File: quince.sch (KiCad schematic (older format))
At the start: 26 parts, among them J1 NEIGHBOR1, J2 NEIGHBOR2, J7 BONUS_ROW, P9 BASEBAND, U1 TLV3502

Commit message: updated to KiCad 5.1
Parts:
- C1: symbol C -> Device:C
- J1, J2: symbol CONN_02X20 -> Connector_Generic:Conn_02x20_Odd_Even
- J7: symbol CONN_01X20 -> Connector_Generic:Conn_01x20
- MH1, MH2, MH3, MH4: symbol CONN_01X01 -> Connector_Generic:Conn_01x01
- P9: symbol CONN_02X08 -> Connector_Generic:Conn_02x08_Odd_Even
- R1, R10, R11, R12, R13, R14, R15, R16, R2, R3, R4, R5, R6, R7, R8, R9: symbol R -> Device:R
- U1: symbol TLV3502 -> gsg-symbols:TLV3502
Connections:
- wire segments 169 -> 188

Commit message: add RF section to schematic copied from Daisho/rx2400ism
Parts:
- removed P9: BASEBAND, gsg-modules:HEADER-2x8, symbol Connector_Generic:Conn_02x08_Odd_Even
- removed R10, R11, R12, R13, R14, R15, R16, R7, R8, R9: R, gsg-modules:0603, symbol Device:R
- added C? (x8): 100nF, symbol Device:C
- added C? (x4): 18pF, symbol Device:C
- added C? (x4): 68pF, symbol Device:C
- added C? (x10): 100pF, symbol Device:C
- added C? (x2): 1pF, symbol Device:C
- added C? (x2): 470pF, symbol Device:C
- added D?: D_TVS, symbol Device:D_TVS
- added FB?: Ferrite_Bead, symbol Device:Ferrite_Bead
- added J? (x2): RFIN, symbol Connector:Conn_Coaxial
- added J?: GND, symbol Connector_Generic:Conn_01x02
- added J? (x11): Conn_01x01, symbol Connector_Generic:Conn_01x01
- added L? (x5): 470nH, symbol Device:L
- added L? (x2): 680nH, symbol Device:L
- added R? (x2): 10k, symbol Device:R
- added R? (x5): 0, symbol Device:R
- added R? (x4): 100, symbol Device:R
- added R? (x2): 2k2, symbol Device:R
- added R? (x2): 3k3, symbol Device:R
- added R? (x2): 200, symbol Device:R
- added R?: 0, gsg-modules:0603, symbol Device:R
- added U2: AD8347, symbol gsg-symbols:AD8347
- added U3: B9413, symbol gsg-symbols:B9413
- added U4: MAX2641, symbol gsg-symbols:MAX2641
- added U5: 2450BP39D100CE, symbol gsg-symbols:2450BP39D100CE
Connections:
- net labels added: +3.3V, +5V, ENBL, IAIN, IMXO, IOFS, IOPN, IOPP, LOIN, LOIP, QAIN, QMXO, QOFS, QOPN, QOPP, RFIN, RFIP, VAGC, VCMO, VDT1, VDT2, VGIN, VREF
- net labels removed: RXBBI+, RXBBI-, RXBBQ+, RXBBQ-, VBUS
- wire segments 188 -> 386
- no-connect marks 96 -> 90
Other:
- note added: "-8 dBm optimal LO power"
- note added: "1.2 V p-p output\n1.0 V common mode"
- note added: "13.5 dB gain"
- note added: "45 MHz low pass baseband filter"
- note added: "Interpret SGPIO0 as I and\nSGPIO1 as Q to reverse\nspectrum inversion caused\nby inversion of U2 Q output."
- note added: "Q channel inverted"
- note added: "TODO\nLO synthesizer with LPC4330 reference clock option\nI2C I/O expander\nmaybe 3.3 V voltage regulator\n"
- note added: "VGIN DAC/ADC option"
- note added: "external LO option"
- note added: "test points"
- moved on the sheet: C1, J1, J2, J7, MH1, MH2, MH3, MH4, R1, R2, R3, R4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

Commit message: add frequency synthesizer
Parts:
- added C?: 10nF, symbol Device:C
- added C?: 10uF, symbol Device:C
- added C? (x2): 100pF, symbol Device:C
- added C? (x4): 100nF, symbol Device:C
- added C? (x2): 1nF, symbol Device:C
- added C? (x2): C, symbol Device:C
- added C?: 560pF, symbol Device:C
- added C?: 270pF, symbol Device:C
- added C?: 8.2nF, symbol Device:C
- added J? (x4): Conn_01x01, symbol Connector_Generic:Conn_01x01
- added R?: 3k3, symbol Device:R
- added R? (x3): 51, symbol Device:R
- added R? (x2): 0, symbol Device:R
- added R?: 1.5k, symbol Device:R
- added R?: 3k, symbol Device:R
- added U6: ADF4360, symbol gsg-symbols:ADF4360
- added X?: TCXO, symbol gsg-symbols:FOX924B
- R?: Note DNP -> (none)
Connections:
- net +3V3: now also C?.1, C?.1, C?.1, C?.2, R?.1, R?.2, R?.2, U6.2 (AVDD), U6.21 (DVDD), U6.6 (VVCO)
- net CLK0: now also C?.2
- net ENBL: now also R?.2
- net GND: now also C?.1, C?.1, C?.1, C?.2, C?.2, C?.2, C?.2, C?.2, R?.1, R?.2, R?.2, U6.0 (EP), U6.1 (CPGND), U6.10 (AGND), U6.11 (AGND), U6.15 (DGND), U6.22 (AGND), U6.3 (AGND), U6.8 (AGND), U6.9 (AGND), X?.2 (GND)
- net LOIN: now also C?.2
- net LOIP: now also C?.2
- net P1_19: now also U6.17 (CLK)
- net P1_20: now also U6.19 (LE)
- net P1_4: now also U6.18 (DATA)
- new net: C?.1, U6.12 (CC)
- new net: R?.1, U6.13 (RSET)
- new net: C?.1, U6.14 (CN)
- new net: C?.2, C?.2, R?.2, U6.24 (CP)
- new net: C?.1, R?.1, U6.4 (RFOUTA)
- new net: C?.1, R?.1, U6.5 (RFOUTB)
- new net: C?.1, X?.3 (OUT)
- new net: C?.1, R?.2, X?.4 (VCC)
- new net: C?.1, C?.2, R?.2
- new net: C?.1, R?.1
- new net CE: J?.1 (Pin_1), R?.1, U6.23 (CE)
- new net MUXOUT: J?.1 (Pin_1), U6.20 (MUXOUT)
- new net REFIN: C?.1, C?.2, C?.2, J?.1 (Pin_1), U6.16 (REFIN)
- new net VTUNE: C?.2, J?.1 (Pin_1), R?.1, U6.7 (VTUNE)
- no-connect marks 90 -> 86
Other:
- note added: "12 MHz"
- note added: "TODO\nI2C I/O expander\nmaybe 3.3 V voltage regulator\n"
- note added: "option to use LPC4330\nCLKOUT as reference clock"
- note removed: "TODO\nLO synthesizer with LPC4330 reference clock option\nI2C I/O expander\nmaybe 3.3 V voltage regulator\n"
- moved on the sheet: C1, C?, D?, FB?, J7, J?, L?, R1, R2, R3, R4, R5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

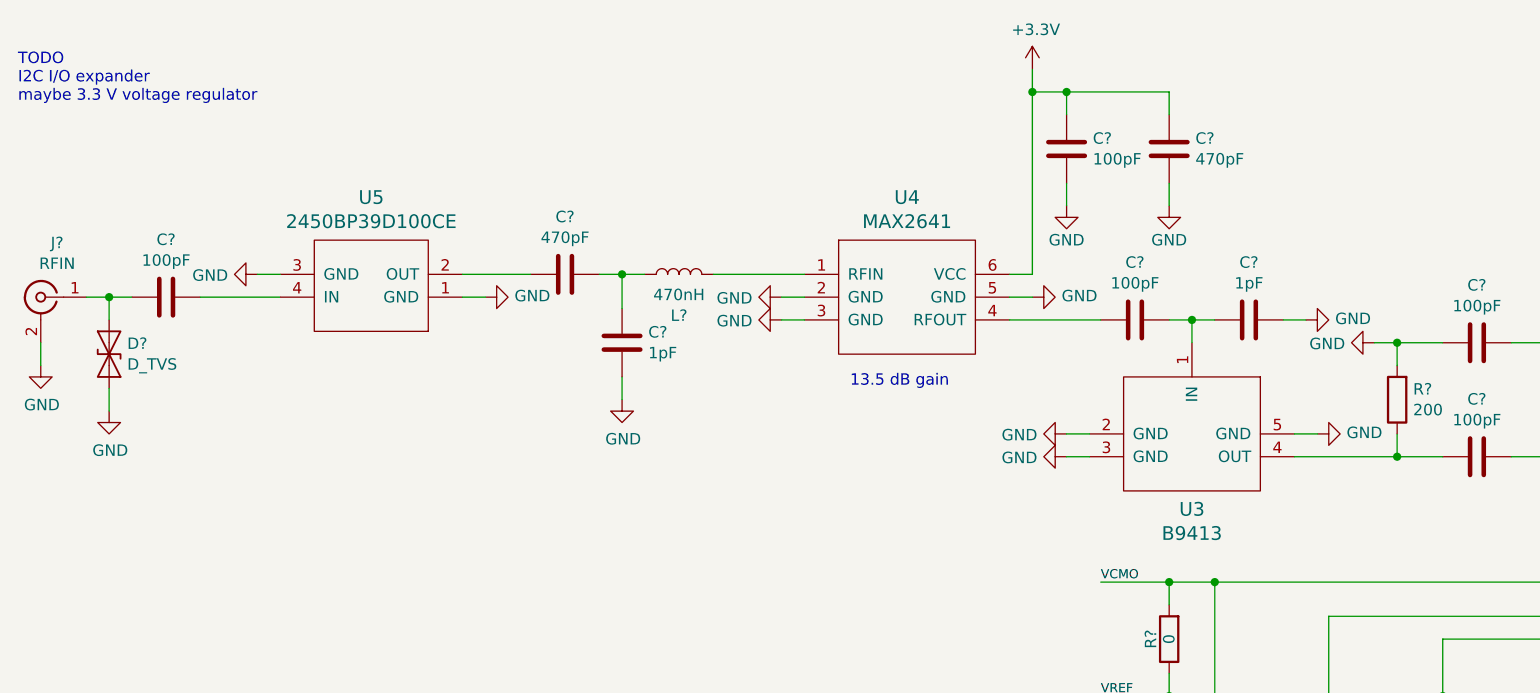
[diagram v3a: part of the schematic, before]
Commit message: change U4 LNA from MAX2641 to BGA5H1BN6 to reduce cost and part count
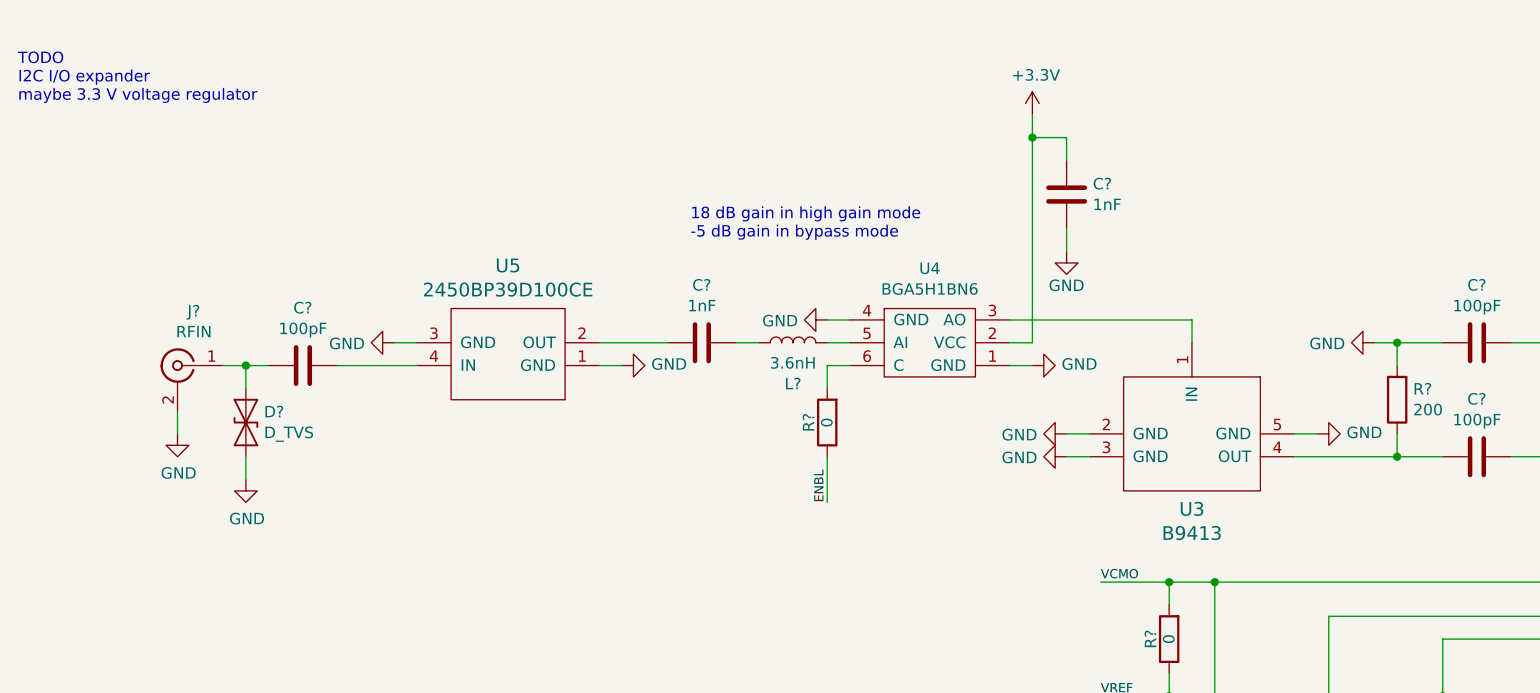
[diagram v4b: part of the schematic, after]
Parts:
- removed C? (x2): 1pF, symbol Device:C
- removed C?: 100pF, symbol Device:C
- removed C?: 470pF, symbol Device:C
- removed U4: MAX2641, symbol gsg-symbols:MAX2641
- added R?: 0, gsg-modules:0603, symbol Device:R
- added U4: BGA5H1BN6, symbol gsg-symbols:BGA5H1BN6
- C?: value 100pF -> 1nF
- C?: value 470pF -> 1nF
- L?: value 470nH -> 3.6nH
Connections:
- net +3V3: now also U4.2 (VCC)
- net ENBL: now also R?.1
- net GND: now also U4.1 (GND), U4.4 (GND)
- net at U3.1 (IN): now also U4.3 (AO)
- net at L?.1: now also U4.5 (AI)
- new net: R?.2, U4.6 (C)
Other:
- note added: "18 dB gain in high gain mode\n-5 dB gain in bypass mode"
- note removed: "13.5 dB gain"
- moved on the sheet: C?, D?, J?, L?, U5

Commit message: assign footprints
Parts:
- C1: value C -> 100nF; footprint gsg-modules:0603 -> gsg-modules:0402
- C10, C11, C12, C13, C14, C15, C16, C17, C18, C19, C2, C20, C21, C22, C23, C24, C25, C26, C27, C28, C29, C3, C30, C31, C32, C33, C34, C35, C36, C38, C39, C4, C40, C41, C42, C5, C6, C7, C8, C9: renamed from C?; footprint (none) -> gsg-modules:0402
- C37: renamed from C?; footprint (none) -> gsg-modules:0805
- D1: renamed from D?; footprint (none) -> gsg-modules:0402
- FB1: renamed from FB?; footprint (none) -> gsg-modules:0805
- J1, J2: Note Alternate: https://www.adafruit.com/products/2223 -> (none)
- J10, J11, J12, J13, J14, J15, J16, J17, J18, J20, J21, J4, J5, J6, J9: renamed from J?; footprint (none) -> gsg-modules:TESTPOINT-50MIL
- J19: renamed from J?; footprint (none) -> gsg-modules:HEADER-1x2
- J3: renamed from J?; footprint (none) -> gsg-modules:SMA-EDGE
- J8: renamed from J?; value RFIN -> LO; footprint (none) -> gsg-modules:SMA-VERTICAL
- L1, L2, L3, L4, L5, L6, L7: renamed from L?; footprint (none) -> gsg-modules:0402
- R1, R2, R3, R4, R5, R6: footprint gsg-modules:0603 -> gsg-modules:0402
- R10, R11, R13, R15, R16, R17, R18, R19, R20, R21, R22, R23, R24, R25, R26, R27, R28, R29, R30, R31, R32, R33, R7, R8, R9: renamed from R?; footprint (none) -> gsg-modules:0402
- R12, R14: renamed from R?; footprint gsg-modules:0603 -> gsg-modules:0402
- U1: Description (none) -> IC COMPARATOR R-R HI-SPD SOT23-8; Manufacturer (none) -> Texas Instruments; Part Number (none) -> TLV3502AIDCNR
- U2: footprint (none) -> gsg-modules:TSSOP28; Description (none) -> RF DEMOD IC 800MZ-2.7GHZ 28TSSOP; Manufacturer (none) -> Analog Devices; Part Number (none) -> AD8347ARUZ-REEL7
- U3: value B9413 -> SAW FILTER; footprint (none) -> gsg-modules:B9413; Description (none) -> FILTER SAW 2.442GHZ 5SMD; Manufacturer (none) -> Qualcomm; Part Number (none) -> B39242B9413K610
- U4: value BGA5H1BN6 -> LNA; footprint (none) -> gsg-modules:BGA7H1N6; Description (none) -> C RF AMP LTE 2.3GHZ-2.69GHZ; Manufacturer (none) -> Infineon Technologies; Part Number (none) -> BGA5H1BN6E6327XTSA1
- U5: value 2450BP39D100CE -> BAND PASS FILTER; footprint (none) -> gsg-modules:2450BP39D100C; Description (none) -> RF FILTER BAND PASS 2.45GHZ 1008; Manufacturer (none) -> Johanson Technology Inc.; Part Number (none) -> 2450BP39D100CE
- U6: footprint (none) -> gsg-modules:QFN24-4
- X1: renamed from X?; footprint (none) -> gsg-modules:XTAL5.0x3.2mm
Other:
- note added: "TODO\nI2C I/O expander\nmaybe 3.3 V voltage regulator\nmaybe replace U6 with CC2500"
- note removed: "TODO\nI2C I/O expander\nmaybe 3.3 V voltage regulator\n"
- moved on the sheet: C1, C10, C11, C12, C13, C14, C15, C16, C17, C18, C19, C2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

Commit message: complete layout
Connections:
- net CC: now reaches C29.1, U6.12 (CC)
- net RSET: now reaches R31.1, U6.13 (RSET)
- net CN: now reaches C37.1, U6.14 (CN)
- net CP: now reaches C26.2, C28.2, R27.2, U6.24 (CP)
- net RFOUTA: now reaches C17.1, R28.1, U6.4 (RFOUTA)
- net RFOUTB: now reaches C16.1, R24.1, U6.5 (RFOUTB)
- net +IN_A renamed IN_A+
- net IN_A+: now also U1.2 (-IN_A); no longer U1.1 (+IN_A)
- net +IN_B renamed IN_B+
- net -IN_A renamed IN_A-
- net IN_A-: now also U1.1 (+IN_A); no longer U1.2 (-IN_A)
- net -IN_B renamed IN_B-
- net IOPN renamed IOP_N
- net IOPP renamed IOP_P
- net LOIN renamed LOI_N
- net LOIP renamed LOI_P
- net QOPN renamed QOP_N
- net QOPP renamed QOP_P
- net RFIN renamed RFI_N
- net RFIP renamed RFI_P
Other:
- note added: "Interpret SGPIO0 as Q\nand SGPIO1 as I."
- note added: "both channels inverted"
- note removed: "Interpret SGPIO0 as I and\nSGPIO1 as Q to reverse\nspectrum inversion caused\nby inversion of U2 Q output."
- note removed: "Q channel inverted"
- moved on the sheet: R31
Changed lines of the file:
@@
 $EndComp
 Text Label 10850 3250 0    40   ~ 0
-+IN_A
+IN_A+
 Text Label 10850 3450 0    40   ~ 0
--IN_A
+IN_A-
 Text Label 10850 3750 0    40   ~ 0
-+IN_B
+IN_B+
 Text Label 10850 3950 0    40   ~ 0
--IN_B
+IN_B-
 $Comp
 L Device:R R1
@@
 	12350 3650 12950 3650
 Wire Wire Line
-	10750 3450 11100 3450
+	10750 3450 11350 3450
 Wire Wire Line
 	10750 3750 11100 3750
@@
 	11100 3650 11100 3750
 Wire Wire Line
-	11250 3250 11250 3450
-Wire Wire Line
 	13350 3450 13550 3450
 Wire Wire Line
@@
 NoConn ~ 16300 8750
 Wire Wire Line
-	11100 3450 11100 3550
-Wire Wire Line
 	12450 3450 12550 3450
 $Comp
@@
 	10750 3950 11250 3950
 Wire Wire Line
-	11100 3550 11350 3550
-Wire Wire Line
-	11250 3450 11350 3450
-Wire Wire Line
 	11250 3750 11350 3750
 Wire Wire Line
@@
 	8250 4700 8250 4900
 Text Label 10000 5050 0    40   ~ 0
-QOPN
+QOP_N
 Text Label 10000 5150 0    40   ~ 0
-QOPP
+QOP_P
 Text Label 10000 2950 0    40   ~ 0
-IOPN
+IOP_N
 Text Label 10000 2850 0    40   ~ 0
-IOPP
+IOP_P
 Text Notes 10450 4200 0    50   ~ 0
-Q channel inverted
+both channels inverted
 Text Notes 10450 3100 0    50   ~ 0
 1.2 V p-p output\n1.0 V common mode
@@
 $EndComp
 Text Label 8350 3200 0    40   ~ 0
-LOIN
+LOI_N
 Text Label 8350 4900 0    40   ~ 0
-LOIP
+LOI_P
 Text Label 8350 5550 0    40   ~ 0
 QAIN
@@
 IMXO
 Text Label 7050 2400 0    40   ~ 0
-RFIP
+RFI_P
 Text Label 7050 1900 0    40   ~ 0
-RFIN
+RFI_N
 Text Label 4950 5600 0    40   ~ 0
 VAGC
@@
 $EndComp
 Text Notes 12900 3250 0    50   ~ 0
-Interpret SGPIO0 as I and\nSGPIO1 as Q to reverse\nspectrum inversion caused\nby inversion of U2 Q output.
+Interpret SGPIO0 as Q\nand SGPIO1 as I.
 Text Notes 3150 1450 0    50   ~ 0
 18 dB gain in high gain mode\n-5 dB gain in bypass mode
@@
 $EndComp
 Wire Wire Line
-	10750 8450 10650 8450
+	10650 8450 10550 8450
 $Comp
 L power:GND #PWR061
 U 1 1 60AA0B62
-P 10650 8450
-F 0 "#PWR061" H 10650 8200 50  0001 C CNN
-F 1 "GND" H 10655 8277 50  0000 C CNN
-F 2 "" H 10650 8450 50  0001 C CNN
-F 3 "" H 10650 8450 50  0001 C CNN
-	1    10650 8450
+P 10550 8450
+F 0 "#PWR061" H 10550 8200 50  0001 C CNN
+F 1 "GND" H 10555 8277 50  0000 C CNN
+F 2 "" H 10550 8450 50  0001 C CNN
+F 3 "" H 10550 8450 50  0001 C CNN
+	1    10550 8450
 	0    1    1    0
 $EndComp
 Wire Wire Line
-	11150 8450 11050 8450
+	11150 8450 10950 8450
 Wire Wire Line
 	11150 8350 11150 8450
@@
 L Device:R R31
 U 1 1 609FCD71
-P 10900 8450
-F 0 "R31" H 10970 8496 50  0000 L CNN
-F 1 "3k3" H 10970 8405 50  0000 L CNN
-F 2 "gsg-modules:0402" V 10830 8450 50  0001 C CNN
-F 3 "~" H 10900 8450 50  0001 C CNN
-	1    10900 8450
+P 10800 8450
+F 0 "R31" H 10870 8496 50  0000 L CNN
+F 1 "3k3" H 10870 8405 50  0000 L CNN
+F 2 "gsg-modules:0402" V 10730 8450 50  0001 C CNN
+F 3 "~" H 10800 8450 50  0001 C CNN
+	1    10800 8450
 	0    1    1    0
 $EndComp
@@
 	1    0    0    -1
 $EndComp
+Text Label 11350 6050 1    40   ~ 0
+RFOUTA
+Text Label 11250 6050 1    40   ~ 0
+RFOUTB
+Text Label 12400 7400 2    40   ~ 0
+CP
+Text Label 10600 7900 0    40   ~ 0
+CC
+Text Label 10950 8450 0    40   ~ 0
+RSET
+Text Label 11100 8800 0    40   ~ 0
+CN
+Wire Wire Line
+	11250 3250 11250 3550
+Wire Wire Line
+	11250 3550 11350 3550
 $EndSCHEMATC
